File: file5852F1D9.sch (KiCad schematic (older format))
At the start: 4 parts

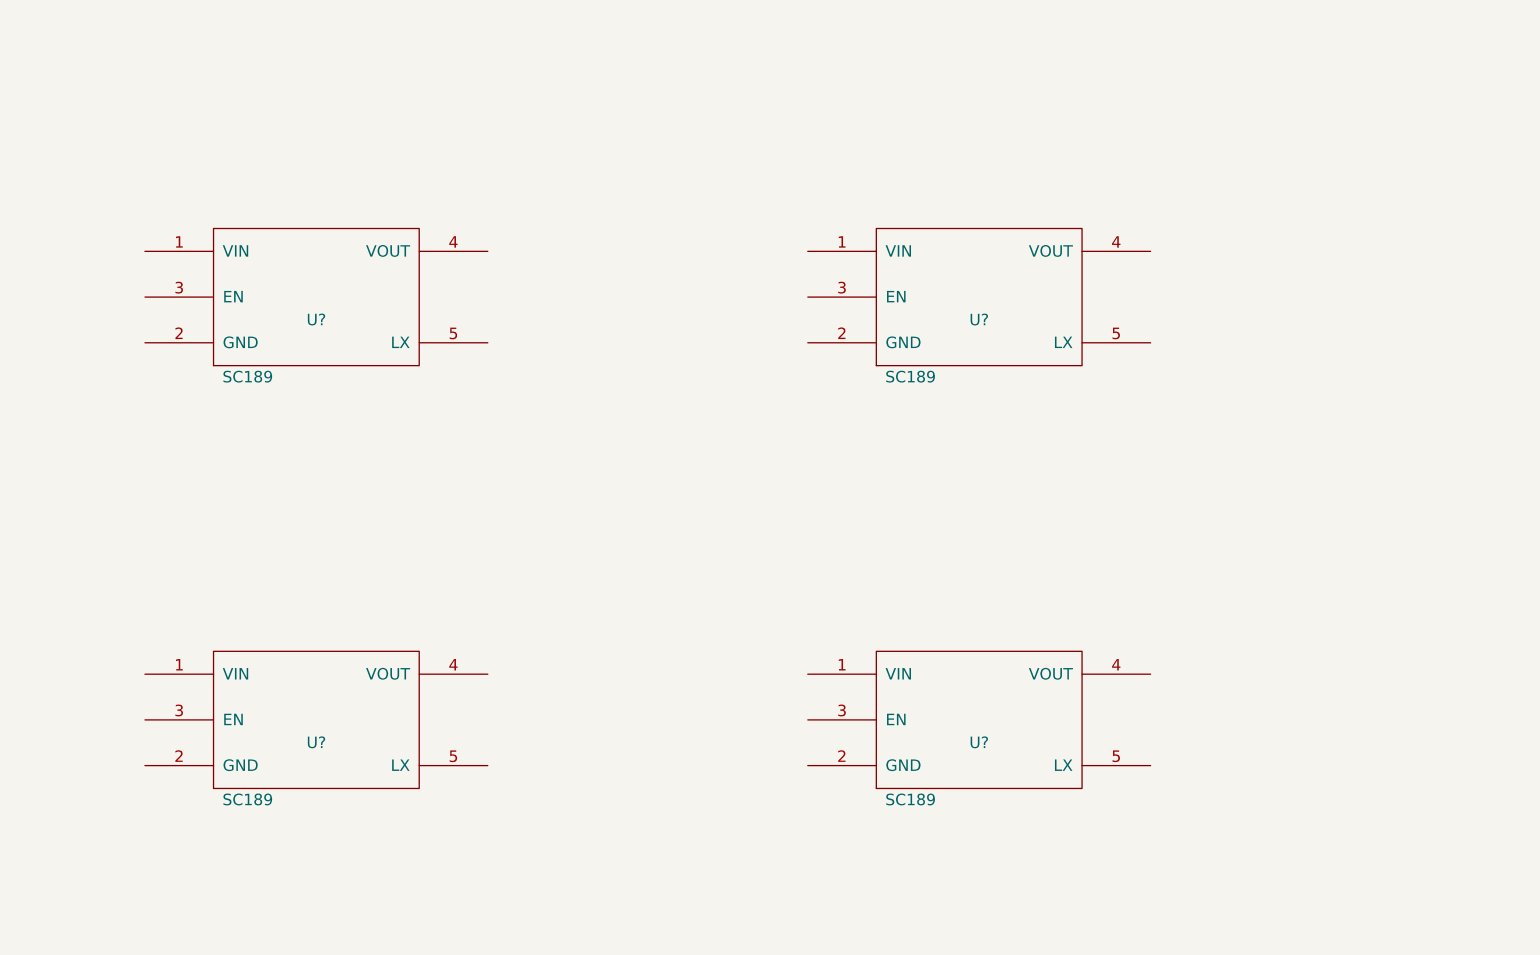
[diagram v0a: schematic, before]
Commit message: added some connections and passives
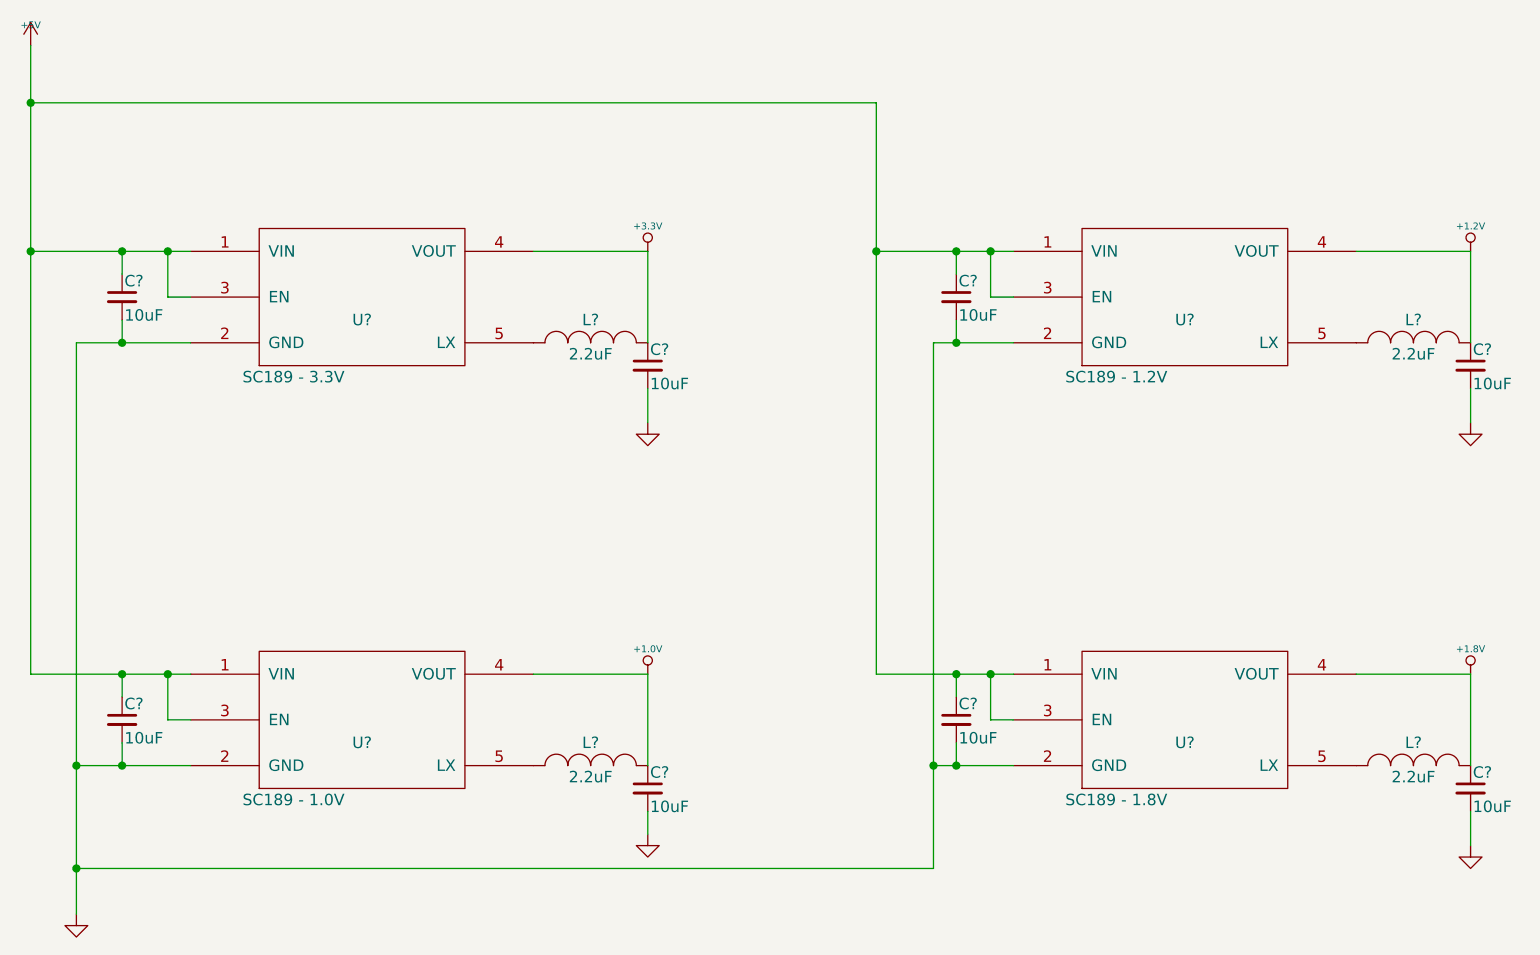
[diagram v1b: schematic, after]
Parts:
- added C? (x8): 10uF, symbol C_Small
- added L? (x4): 2.2uF, symbol INDUCTOR_SMALL
- U?: value SC189 -> SC189 - 1.2V
- U?: value SC189 -> SC189 - 1.8V
- U?: value SC189 -> SC189 - 3.3V
- U?: value SC189 -> SC189 - 1.0V
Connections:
- net +5V: now reaches U?.1 (VIN)
- net +5V: now also U?.1 (VIN), U?.1 (VIN), U?.1 (VIN), U?.3 (EN), U?.3 (EN), U?.3 (EN), U?.3 (EN), C?.1, C?.1, C?.1, C?.1
- net GND: now reaches U?.2 (GND)
- net GND: now also U?.2 (GND), U?.2 (GND), U?.2 (GND), C?.2, C?.2, C?.2, C?.2, C?.2, C?.2, C?.2, C?.2
- net +1.2V: now reaches U?.4 (VOUT)
- net +1.2V: now also C?.1, L?.2
- net at U?.5 (LX): now also L?.1 (x4)
- net +1.8V: now reaches U?.4 (VOUT)
- net +1.8V: now also C?.1, L?.2
- net +3.3V: now reaches U?.4 (VOUT)
- net +3.3V: now also C?.1, L?.2
- net +1.0V: now reaches U?.4 (VOUT)
- net +1.0V: now also C?.1, L?.2
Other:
- moved on the sheet: U?

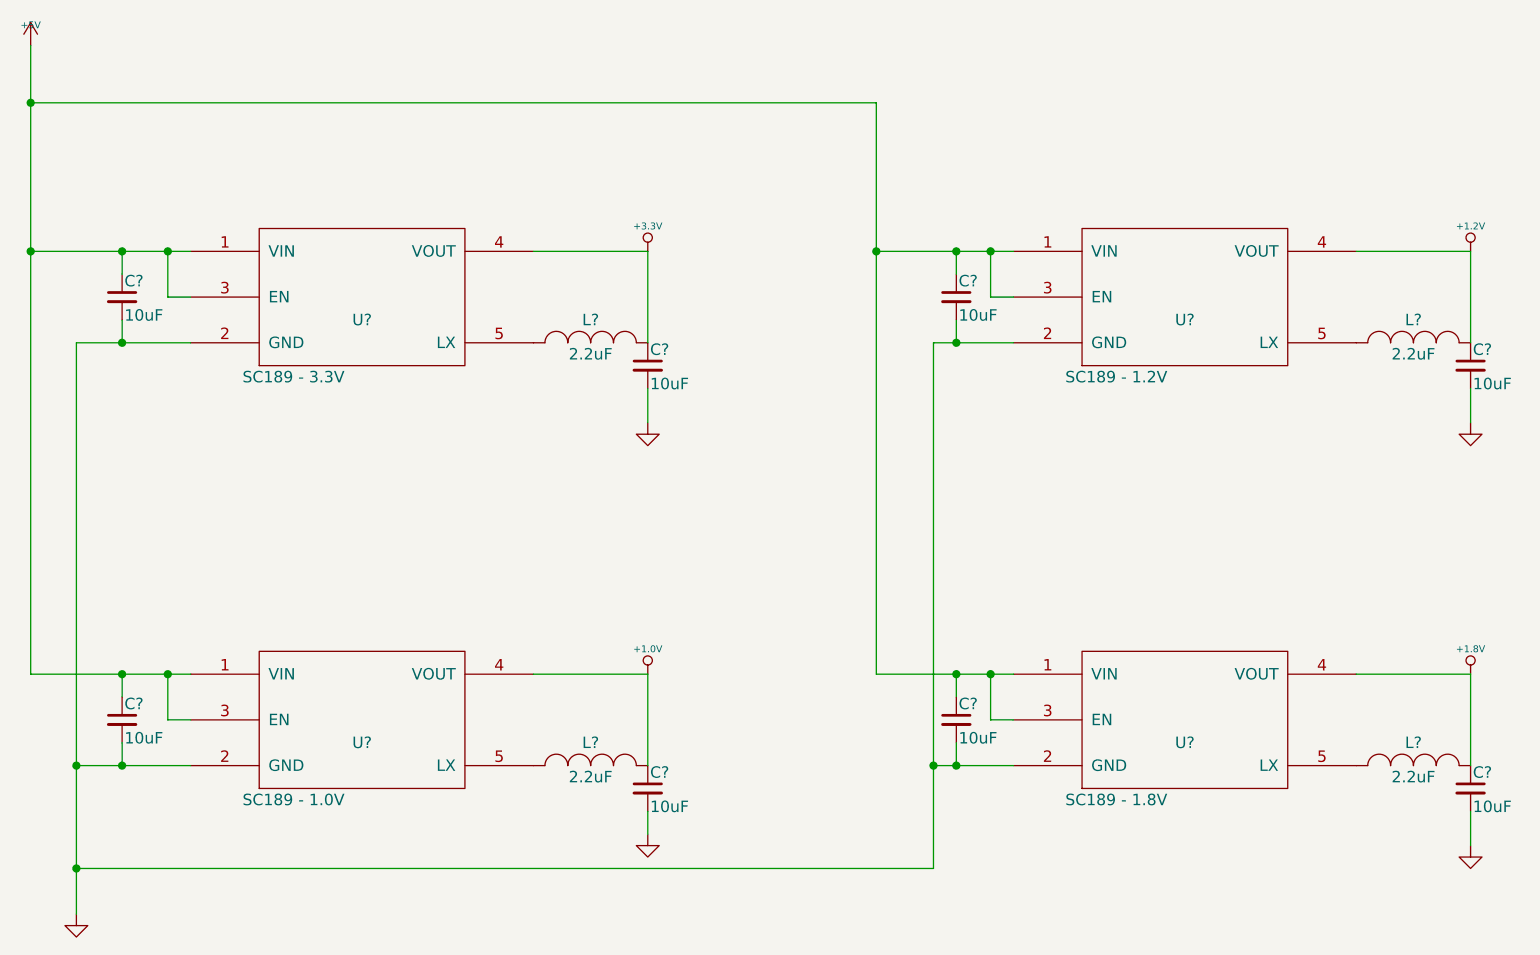
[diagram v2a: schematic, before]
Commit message: finished configuration page of the FPGA
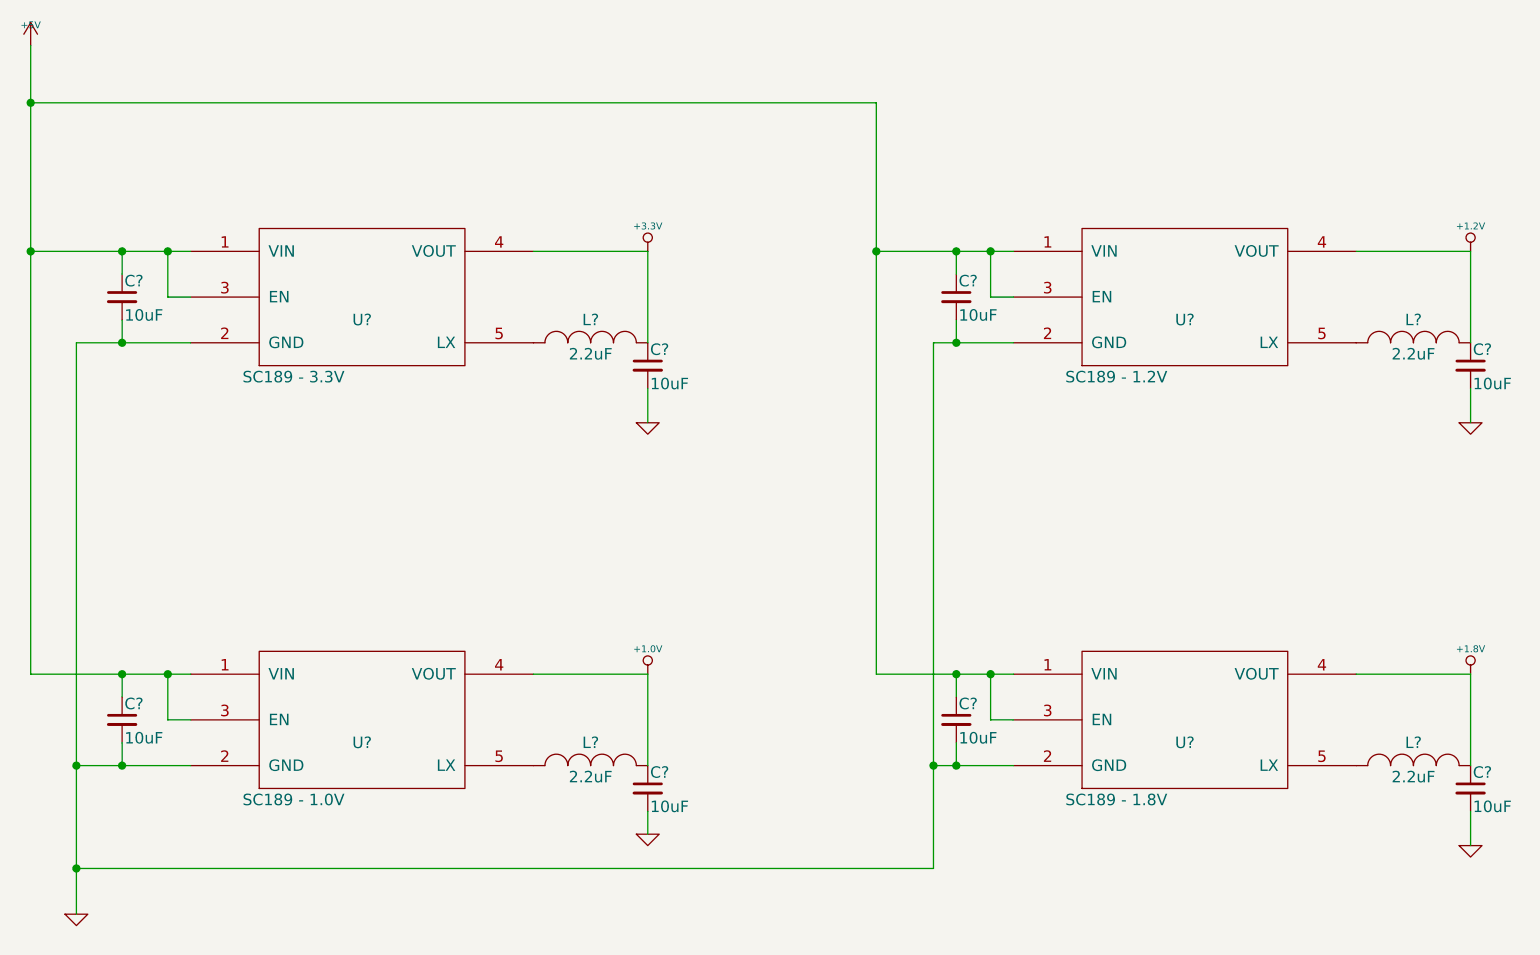
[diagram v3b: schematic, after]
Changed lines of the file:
@@
 EESchema Schematic File Version 2
+LIBS:DFTBoard-rescue
 LIBS:power
 LIBS:device
@@
 LIBS:SC189
 LIBS:s70fl01gs
-LIBS:_sensors
 LIBS:PROpendous-cache
-LIBS:_antenna
-LIBS:_audio
-LIBS:_charge-pump-regulators
-LIBS:_connectors
-LIBS:_discrete
-LIBS:_div
-LIBS:_ic
-LIBS:_linear-regulators
-LIBS:_motor_drivers
-LIBS:_power
-LIBS:_stm32
-LIBS:_transceiver
-LIBS:_wireless
-LIBS:Comp2014
-LIBS:cvra
-LIBS:IRF
 LIBS:logo
-LIBS:Mec
-LIBS:National
-LIBS:phoenix
+LIBS:JTAG
 LIBS:DFTBoard-cache
 EELAYER 25 0
@@
 $Descr A4 11693 8268
 encoding utf-8
-Sheet 9 11
+Sheet 9 12
 Title ""
 Date ""
@@
 Connection ~ 6900 2750
 $Comp
-L GND #PWR?
+L GND-RESCUE-DFTBoard #PWR?
 U 1 1 58592DBB
 P 3400 5650
@@
 	9500 4600 9500 5000
 $Comp
-L GND #PWR?
+L GND-RESCUE-DFTBoard #PWR?
 U 1 1 58594786
 P 5900 3500
@@
 $EndComp
 $Comp
-L GND #PWR?
+L GND-RESCUE-DFTBoard #PWR?
 U 1 1 58594848
 P 5900 5300
@@
 	5900 5200 5900 5300
 $Comp
-L GND #PWR?
+L GND-RESCUE-DFTBoard #PWR?
 U 1 1 58594C14
 P 9500 5350
@@
 $EndComp
 $Comp
-L GND #PWR?
+L GND-RESCUE-DFTBoard #PWR?
 U 1 1 58594C4F
 P 9500 3500
@@
 	9500 5200 9500 5350
 $Comp
-L +3.3V #PWR?
+L +3.3V-RESCUE-DFTBoard #PWR?
 U 1 1 585961A7
 P 5900 2750
